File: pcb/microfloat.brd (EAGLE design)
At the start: 76.2 x 66 mm, 134 parts, among them J1 503182-1852, J11 JTAG-MINI, J2 USB4105_REVA, J3 1054291110, J4 1054291110, J5 1054291116, J9 1909763-1, T1 MMBT3906, U1 BME280, U12 TPS54308DDCT, U13 TPS54308DDCT, U2 ICM-42688-P, U3 MAX13237EETE, U4 NEO-M8N-0, U5 TXB0104PWR, U6 LTC4419CMSEPBF, U7 TPS54308DDCT, U8 TPS54308DDCT, U9 ATSAMD51N20A-AUT, Y1 32.768kHz

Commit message: part of component placement done
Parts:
- removed J11: JTAG-MINI, microfloat:FTSH-105-01-F-D-K
- removed U$16, U$17, U$18: (no value), RoboJackets-Aesthetics:STANDOFF-HOLE
- added C41: 10uF, rcl:E2,5-5
- added C42: 100uF, rcl:E3,5-8
- added C43, C44: 0.1uF, rcl:C0603
- added F6: 0.6A, microfloat:F1206
- added J6: JTAG-MINI, microfloat:FTSH-105-01-F-D-K
- U$15: device RoboJackets-Aesthetics:STANDOFF-HOLE -> microfloat:UCM-MODEM
- moved J4 471.1 mm to (24.2, 67.5)
- moved C26 280.3 mm to (24.0, 25.0), flipped to the bottom, turned to 90 degrees
- moved C27 147.4 mm to (46.2, -204.0)
- moved R6 128.6 mm to (98.2, -35.7)
- moved R7 119.6 mm to (92.8, -24.6)
- moved T1 118.1 mm to (70.9, -82.7)
- moved U9 117.4 mm to (24.0, 30.0)
- moved R2 103.6 mm to (65.1, -65.5)
- moved C14 102.2 mm to (84.4, -53.9)
- moved C1 100.5 mm to (67.5, -73.6)
- moved R5 87.3 mm to (61.1, -56.3)
- moved R4 76.5 mm to (60.6, -42.9)
- moved C3 67.4 mm to (77.7, -21.3)
- moved C5 65.6 mm to (73.9, -21.7)
- moved C4 64.7 mm to (72.6, -24.7)
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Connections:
- removed net GND1: C11.2, C12.2, C29.2, C30.2, C8.2
- new net N$27: C41.+, C42.+, F6.1
- new net N$29: J6.3
- net !RESET: now also J6.10; no longer J11.10
- net +3V3: now also C43.1, C44.1, J6.1; no longer J11.1
- net GND: now also C11.2, C12.2, C29.2, C30.2, C41.-, C42.-, C43.2, C44.2, C8.2, J6.5; no longer J11.3, J11.5
- net SWCLK: now also J6.4; no longer J11.4
- net SWDIO: now also J6.2; no longer J11.2
- net VBATT: now also F6.2
- net XIN32: now also U9.1
- net XOUT32: now also U9.2
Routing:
- net GND: track 98.8 -> 0.00 mm, vias 33 -> 0
- net MISO_2: track 49.4 -> 0.00 mm, vias 6 -> 0
- net SCLK_2: track 45.3 -> 0.00 mm, vias 6 -> 0
- net RAD_BUSY: track 41.6 -> 0.00 mm, vias 2 -> 0
- net MOSI_2: track 40.8 -> 0.00 mm, vias 3 -> 0
- net MOSI_1: track 36.4 -> 0.00 mm, vias 2 -> 0
- net SWDIO: track 35.5 -> 0.00 mm, vias 2 -> 0
- net +3V3: track 32.7 -> 0.00 mm, vias 11 -> 0
- net MISO_1: track 32.5 -> 0.00 mm
- net ANT_SW: track 32.3 -> 0.00 mm, vias 3 -> 0
- net D_N: track 32.2 -> 0.00 mm, vias 2 -> 0
- net LNA_EN: track 31.9 -> 0.00 mm
- net !RESET: track 31.5 -> 0.00 mm, vias 1 -> 0
- net SWCLK: track 31.0 -> 0.00 mm
- net SCLK_1: track 31.0 -> 0.00 mm, vias 2 -> 0
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- removed copper zone on layer 1, net +12V
- removed copper zone on layer 1, net +3V3
- removed copper zone on layer 1, net +5V
- removed copper zone on layer 16, net +6V
- removed copper zone on layer 15, net GND
- removed copper zone on layer 2, net VBATT
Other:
- board size 76.2 x 66 mm -> 76.2 x 60.3 mm

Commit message: component placement near complete, need to fix connector, place test points
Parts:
- moved F6 544.7 mm to (-1.92, 46.1), flipped to the bottom, turned to 180 degrees
- moved C42 538.1 mm to (-6.35, 48.3)
- moved C41 537.4 mm to (-2.72, 54.1)
- moved R30 525.9 mm to (15.2, 43.8), flipped to the bottom, turned to 90 degrees
- moved R29 520.3 mm to (12.5, 43.8), flipped to the bottom, turned to 270 degrees
- moved C40 508.1 mm to (50.3, 24.2), flipped to the bottom, turned to 90 degrees
- moved C31 494.0 mm to (39.5, 18.1), flipped to the bottom
- moved R28 489.2 mm to (22.6, 51.7), flipped to the bottom, turned to 180 degrees
- moved C30 487.8 mm to (12.6, 25.3), flipped to the bottom, turned to 270 degrees
- moved C29 482.3 mm to (10.4, 25.3), flipped to the bottom, turned to 270 degrees
- moved J5 479.8 mm to (14.1, 63.7), flipped to the bottom
- moved F5 475.1 mm to (53.3, 21.2), flipped to the bottom
- moved R27 443.3 mm to (2.73, 41.5), flipped to the bottom, turned to 270 degrees
- moved R3 435.5 mm to (2.27, 38.8), flipped to the bottom, turned to 180 degrees
- moved CR1 434.7 mm to (2.00, 44.9), flipped to the bottom, turned to 90 degrees
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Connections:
- removed net N$25: R14.2, R15.2, R16.2, R17.2, R18.2
- net +3V3: now also R14.2, R15.2, R16.2, R17.2, R18.2

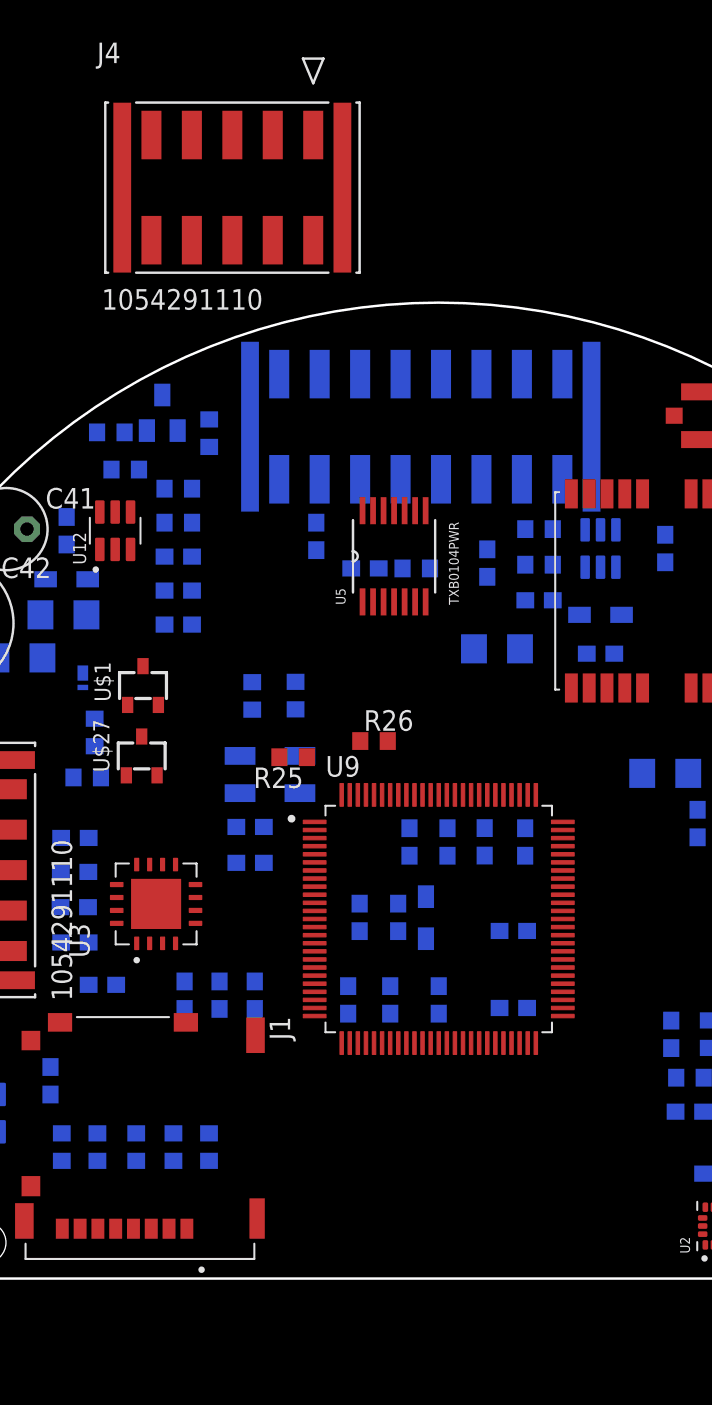
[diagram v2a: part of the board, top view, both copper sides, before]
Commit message: removed values and moved stuff to top
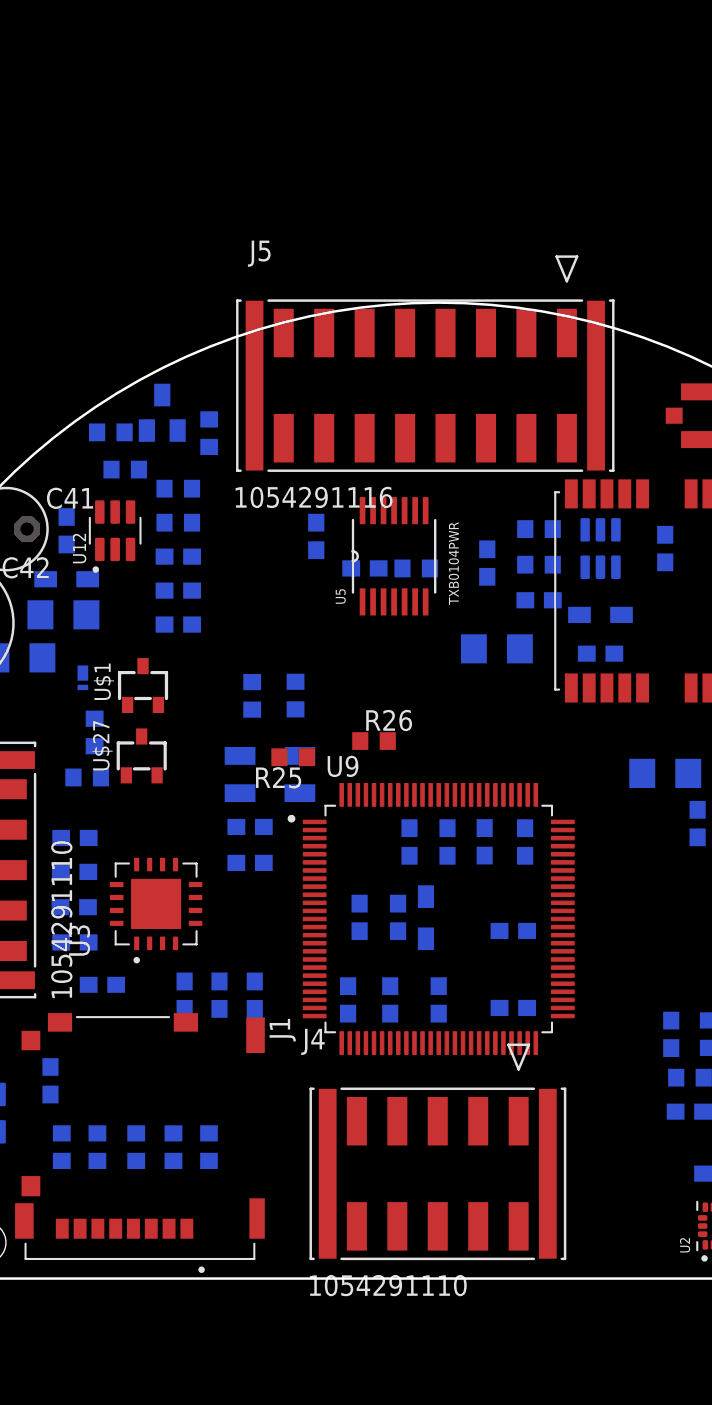
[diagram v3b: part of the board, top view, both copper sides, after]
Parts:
- moved J4 62.3 mm to (28.9, 17.5)
- moved J5 18.0 mm to (31.9, 66.2), flipped to the top

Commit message: Work in progress
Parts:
- removed L1: 380hm, RoboJackets-Inductors:0805
- added C45, C46: 0.1uF, rcl:C0603
- C15, C16: value 15 pF -> 8.2 pF
- F6: value 0.6A -> 3A
- moved U5 5.24 mm to (20.0, 47.3)
- moved J5 3.81 mm to (31.9, 62.4)
- moved U4 3.81 mm to (39.2, 46.5)
- moved C42 2.24 mm to (-4.35, 47.3)
- moved F6 2.00 mm to (-1.92, 44.1)
- moved U$15 0.22 mm to (-6.00, 7.78)
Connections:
- removed net N$29: J6.3
- removed net N$30: J4.11
- net +3V3: now also C36.1, C37.1, C45.1, C46.1; no longer L1.1
- net GND: now also C45.2, C46.2, J4.11, J6.3
- net VCCA: no longer C36.1, C37.1, L1.2
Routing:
- net GND: track 0.00 -> 47.4 mm, vias 0 -> 18
- net +3V3: track 0.00 -> 3.18 mm, vias 0 -> 1
- added copper zone on layer 15, net +3V3
- added copper zone on layer 2, net GND

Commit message: Put final crystal part
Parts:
- added C47: 10uF, rcl:C0603
- added C48: 0.1uF, rcl:C0603
- added L1: FB-30Ohm, RoboJackets-Inductors:0805
- added L4: 10uH, RoboJackets-Inductors:0805
- C36: value 0.1uF -> 10uF
- moved U9 0.25 mm to (24.0, 29.8)
- moved U4 0.22 mm to (39.2, 46.2)
- flipped U$1 to the bottom
- flipped U$27 to the bottom
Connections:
- new net GND1: C47.2
- new net GND2: C48.2
- new net N$25: L4.1, U9.91
- net +3V3: now also L1.1
- net VCCA: now also C47.1, C48.1, L1.2
- net VCC_CORE: now also L4.2
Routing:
- net SOLENOID: track 0.00 -> 34.7 mm, vias 0 -> 1
- net GND: track 47.4 -> 63.4 mm, vias 18 -> 25
- net GPS_ANT: track 0.00 -> 11.3 mm
- net N$24: track 0.00 -> 4.61 mm
- net SOL_TRIG: track 0.00 -> 3.90 mm

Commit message: Final schematic with missing passives
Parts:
- removed C56: 22uF, rcl:C0603
- removed J5: 1054291116, microfloat:CON_1054291116_MOL
- removed S2: KMR2, RoboJackets-Switches:KMR2
- added BT1: BATTERY, microfloat:BR-1632A/HAN
- added C49: 0.1uF, rcl:C0603
- added C50: 10uF, rcl:C0603
- added C51: 1.0uF, rcl:C0603
- added C52: 22uF, rcl:C0603
- added J7, J8: 1054291110, microfloat:CON_1054291110_MOL
- added R35: 330, rcl:R0603
- added S1: (no value), microfloat:TACTILE_SWITCH_SMD_6.2MM_TALL
- R19: value 10k -> 1k
- Y1: value 32.768kHz -> ABS25-32.768KHZ-6-1-T; device microfloat:CRYSTAL-SMD-5X3 -> microfloat:XTAL_ABS25-32.768KHZ-6-1-T
- moved C55 273.8 mm to (-20.0, -220.0), flipped to the top
- moved C37 203.9 mm to (-20.0, -170.0), flipped to the top, turned to 0 degrees
- moved C36 199.5 mm to (-20.0, -165.0), flipped to the top, turned to 0 degrees
- moved C35 196.1 mm to (-20.0, -155.0), flipped to the top, turned to 0 degrees
- moved C26 170.8 mm to (-20.0, -140.0), flipped to the top, turned to 0 degrees
- moved Y1 125.2 mm to (-19.0, -82.0), flipped to the top
- moved C47 99.2 mm to (-20.0, -175.0)
- moved C46 94.2 mm to (-20.0, -160.0)
- moved C45 89.2 mm to (-20.0, -150.0)
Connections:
- removed net GND1: C47.2
- removed net GND2: C48.2
- new net !RESET!: R35.2
- new net N$29: R35.1, S1.A1, S1.A2
- new net N$30: J8.11
- new net N$31: J7.11
- new net N$32: BT1.+, U4.22
- new net TX_READY: U4.4, U9.78
- net !RESET: no longer S2.1, S2.3
- net +12V: now also J7.8; no longer J5.14
- net +3V3: now also C49.1, C50.1, C51.1; no longer U4.22
- net GND: now also BT1.-, C47.2, C48.2, C49.2, C50.2, C51.2, C52.2, J7.1, J7.12, J7.2, J7.6, J7.7, J7.9, J8.12, S1.B1, S1.B2; no longer C56.2, J5.12, J5.13, J5.15, J5.17, J5.18, J5.4, J5.5, S2.2, S2.4
- net N$17: now also C52.1; no longer C56.1
- net PROBE: now also J8.4, J8.9; no longer J5.11, J5.3
- net RREF+: now also J8.2; no longer J5.1
- net RREF-: now also J8.7; no longer J5.9
- net RSENSE+: now also J8.3; no longer J5.2
- net RSENSE-: now also J8.8; no longer J5.10
- net SOL_TRIG: now also J7.3; no longer J5.6
- net UART_RX_M_B: now also J7.4; no longer J5.7
- net UART_TX_M_B: now also J7.5; no longer J5.8
- net VBATT: now also J7.10; no longer J5.16
- net XOUT32: now also Y1.4; no longer Y1.3
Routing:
- net GND: track 63.4 -> 41.2 mm, vias 25 -> 17

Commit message: More placement
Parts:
- moved J8 189.7 mm to (20.8, 61.5)
- moved J7 175.4 mm to (37.2, 61.5)
- moved J9 2.24 mm to (42.1, 60.1)
- moved U5 1.27 mm to (20.0, 46.1)
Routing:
- net GPS_ANT: track 11.3 -> 0.00 mm
- net GND: track 41.2 -> 42.2 mm

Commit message: Swapped capcitors into parallel
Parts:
- removed C11, C12, C8: 0.2 uF, rcl:C0603
- added C56, C61, C62, C63, C64, C65, C66, C67, C68: 0.1uF, rcl:C0603
- C10, C7, C9: value 0.2 uF -> 0.1uF
- moved C7 340.5 mm to (-20.0, -314.0), flipped to the top, turned to 0 degrees
- moved C9 273.4 mm to (-20.0, -244.0), flipped to the top, turned to 0 degrees
- moved C10 261.0 mm to (-20.0, -234.0), flipped to the top, turned to 0 degrees
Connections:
- net +3V3: now also C64.1, C67.1, C68.1, C7.1; no longer C11.1, C12.1
- net GND: now also C56.2, C61.2, C64.2, C65.2, C66.2, C67.2, C68.2; no longer C11.2, C12.2, C8.2
- net N$10: now also C65.1, C66.1; no longer C8.1
- net N$2: now also C63.1
- net N$4: now also C63.2
- net N$5: now also C62.1
- net N$6: now also C62.2
- net N$8: now also C56.1, C61.1; no longer C7.1
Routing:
- net SOLENOID: track 34.7 -> 0.00 mm, vias 1 -> 0
- net GND: track 42.2 -> 14.4 mm, vias 17 -> 7
- net N$24: track 4.61 -> 0.00 mm
- net SOL_TRIG: track 3.90 -> 0.00 mm
- net +3V3: track 3.18 -> 0.00 mm, vias 1 -> 0
- net N$30: track 0.00 -> 1.66 mm, vias 0 -> 1
- net N$31: track 0.00 -> 1.09 mm, vias 0 -> 1
